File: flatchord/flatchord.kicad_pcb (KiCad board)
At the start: 2 copper layers, 68.6 x 34.3 mm, 9 parts, among them J1 OLED SSD1306, SW0 SW_SPST, SW1 SW_SPST, SW2 SW_SPST, SW3 SW_SPST, SW4 SW_SPST, SW5 SW_DPDT_x2, U2 Nice! Nano (ProMicro)

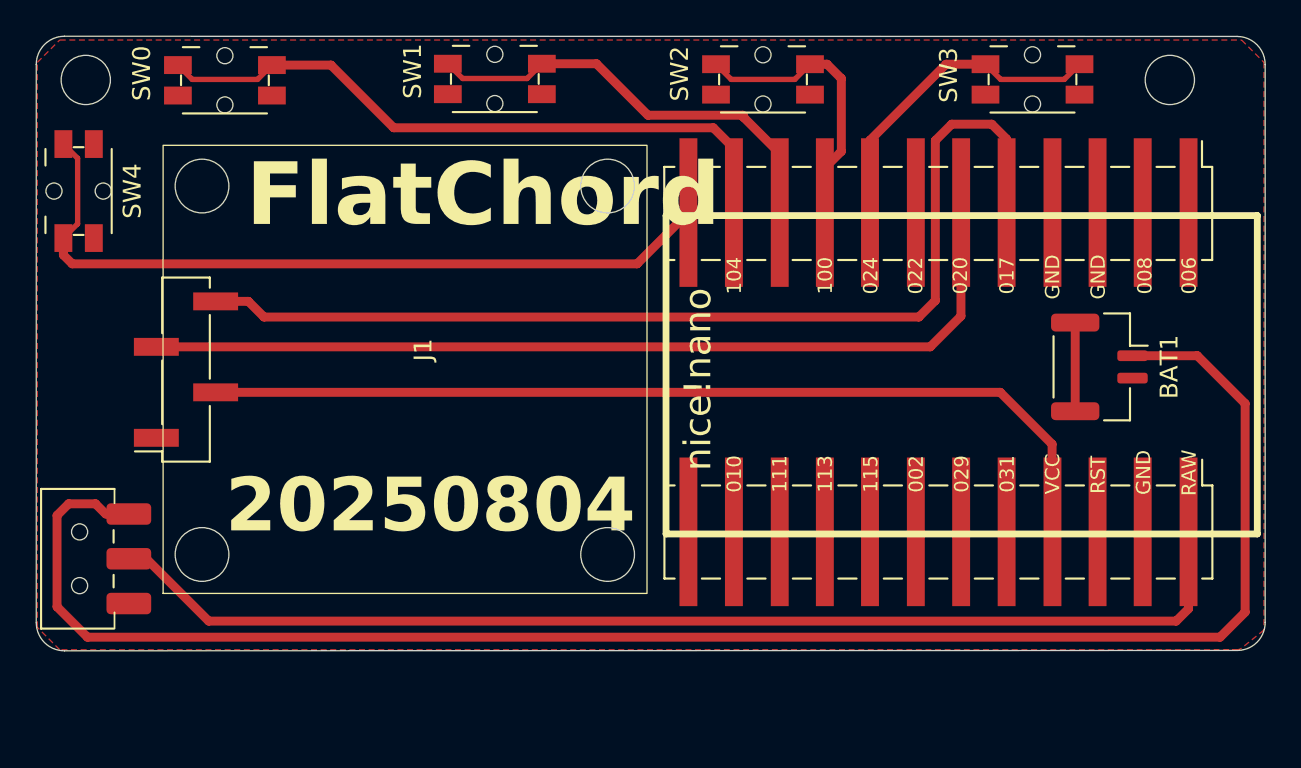
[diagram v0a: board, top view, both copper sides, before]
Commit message: significant changes
new display 1.3" SH1106 and ESP32-S3 supermini, big shrink in size
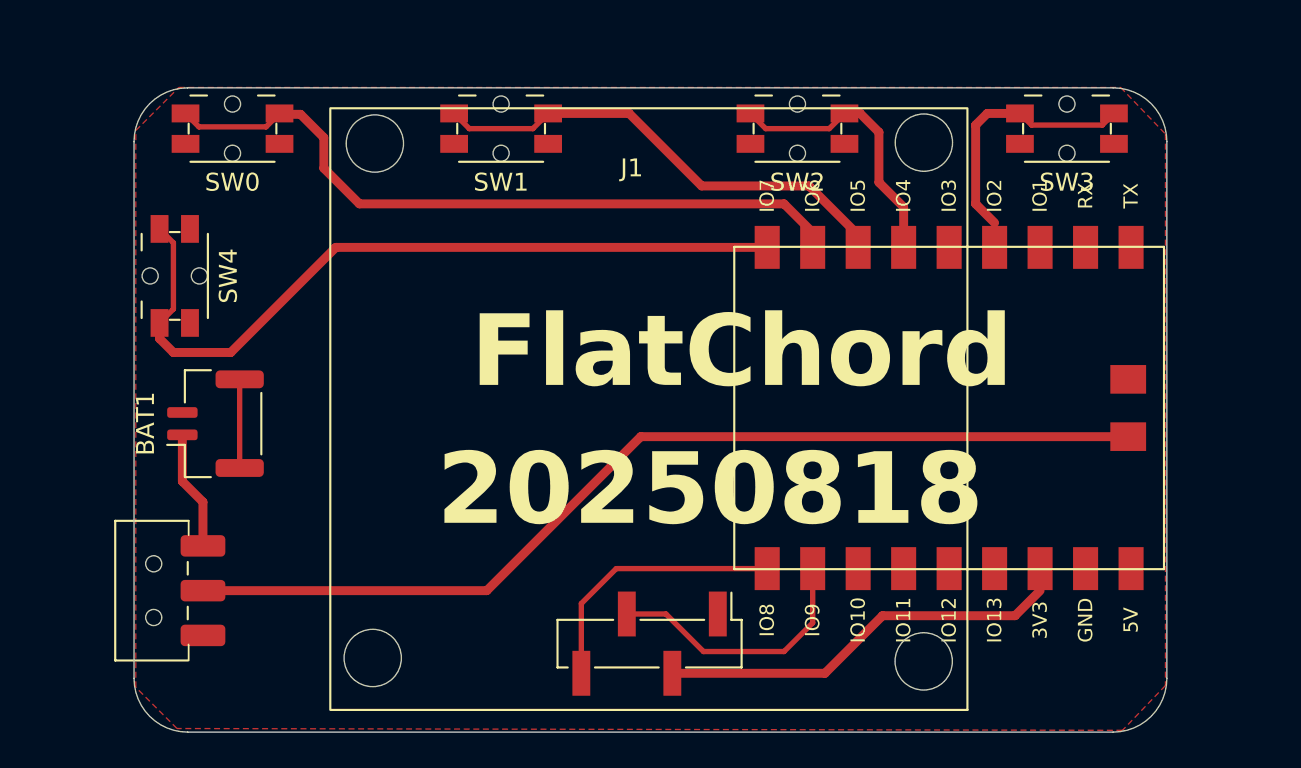
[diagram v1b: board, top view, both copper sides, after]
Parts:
- removed U2: Nice! Nano (ProMicro), footprints:nnv2-smd-2x
- added U1: esp32s3-supermini, footprints:ESP32-S3-SuperMini_SMT, F.Cu at (218.7, 86.4)
- J1: value OLED SSD1306 -> OLED SH1106; footprint ssd1306-smd-header:lightblue-ssd1306-smd -> footprints:tft-sh1106-1.3-i2c
- moved BAT1 49.5 mm to (177.8, 87.3), turned to 90 degrees
- moved J1 14.7 mm to (202.0, 86.5), turned to 180 degrees
- moved SW4 7.16 mm to (175.5, 79.0)
- moved SW5 4.51 mm to (174.6, 96.6)
- moved SW2 3.36 mm to (210.2, 70.8)
- moved SW3 3.36 mm to (225.3, 70.8)
- moved SW1 2.80 mm to (193.7, 70.8)
- moved SW0 2.73 mm to (178.7, 70.8)
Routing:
- net /B+: track 96.3 -> 6.68 mm
- net /SDA: track 56.2 -> 15.1 mm
- net /SCL: track 48.9 -> 14.9 mm
- net VCC: track 50.3 -> 22.5 mm
- net /RAW: track 62.7 -> 55.2 mm
- net /index: track 34.7 -> 39.4 mm
- net /middle: track 22.1 -> 26.1 mm
- net /ring: track 13.4 -> 15.3 mm
- net /pinky: track 15.7 -> 14.4 mm
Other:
- board size 68.6 x 34.3 mm -> 57.7 x 36 mm
- board text added: "20250818"
- board text added: "BAT 150mah 401730"
- board text added: "BAT 220mAh 751424"
- board text removed: "20250804"

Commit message: getting small
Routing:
- net /SCL: track 14.9 -> 19.3 mm
- net /SDA: track 15.1 -> 17.9 mm
- net VCC: track 22.5 -> 24.7 mm

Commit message: ready for prototypes
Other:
- board text added: "20250820"
- board text removed: "20250818"
